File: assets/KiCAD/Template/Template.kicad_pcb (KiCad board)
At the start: 2 copper layers, 96.5 x 96.5 mm, 4 parts

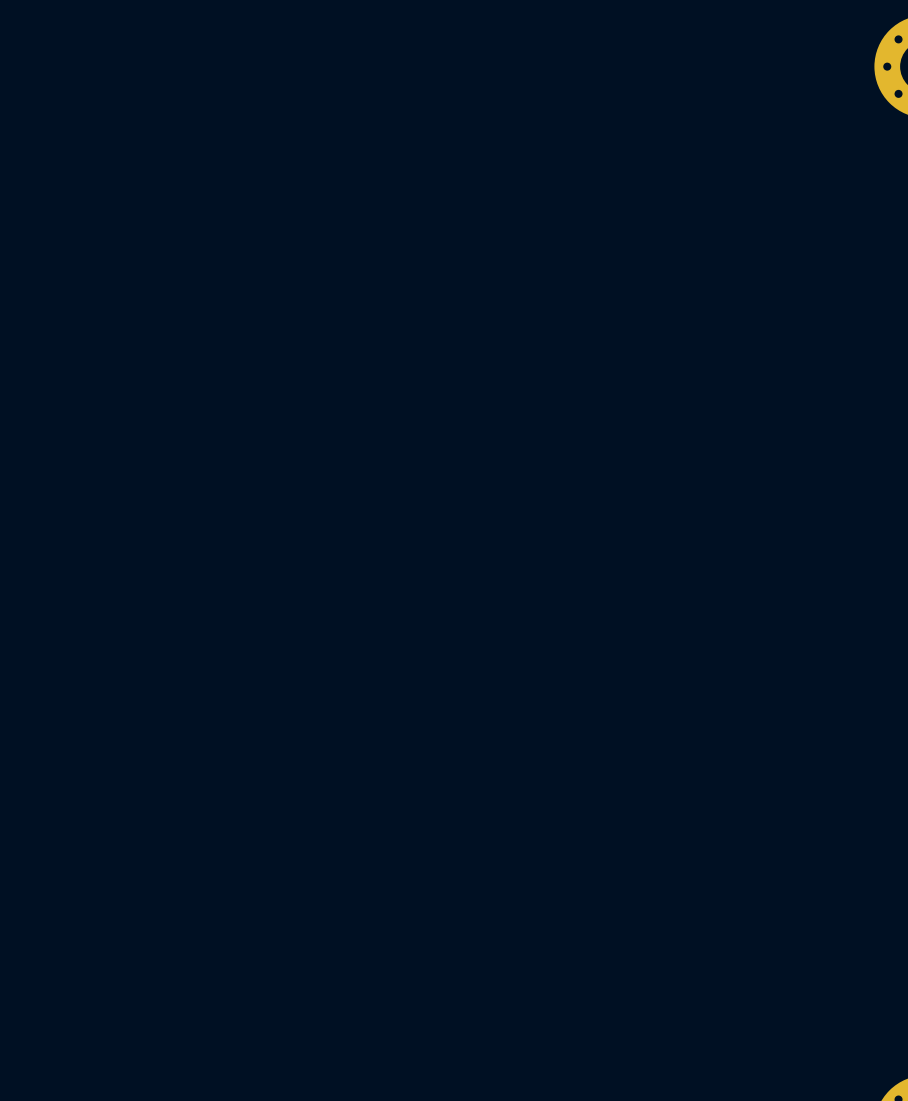
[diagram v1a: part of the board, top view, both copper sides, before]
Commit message: added terrain to opencl
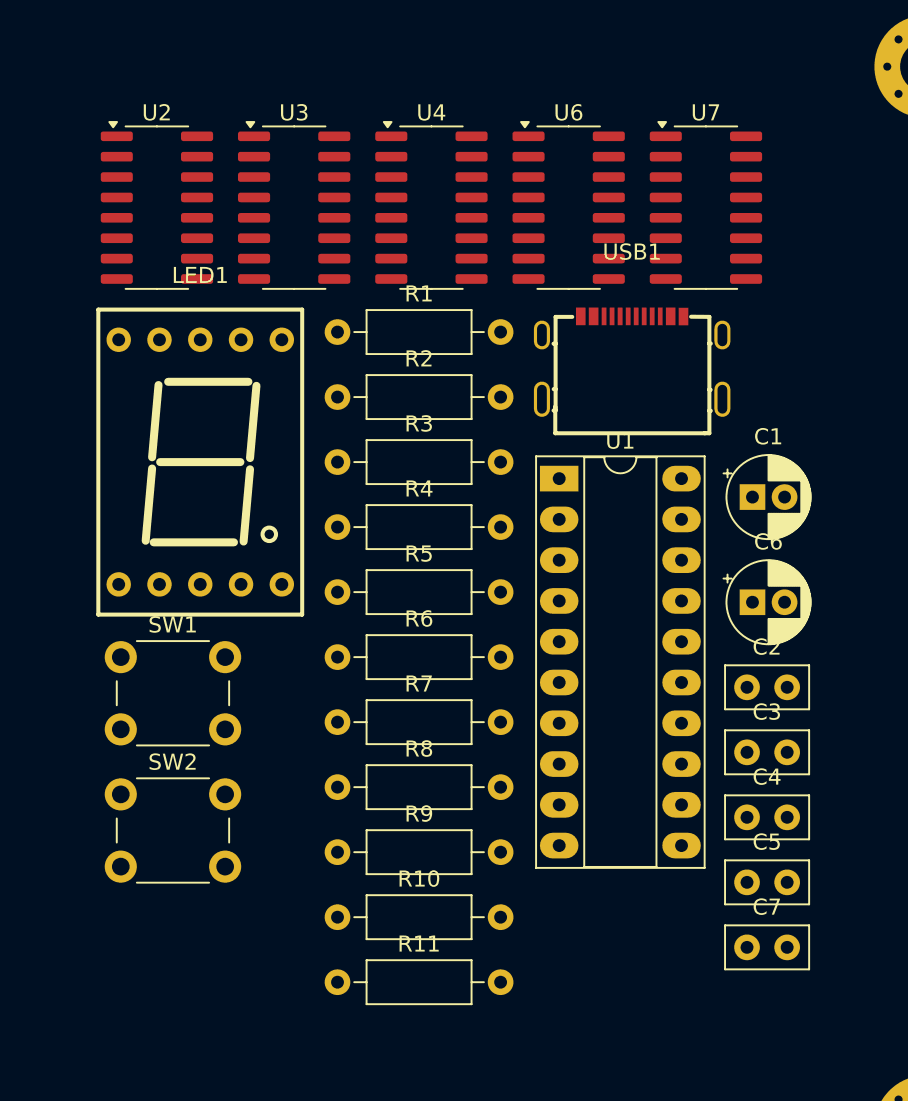
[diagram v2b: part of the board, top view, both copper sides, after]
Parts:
- added C1: 10uF, Capacitor_THT:CP_Radial_D5.0mm_P2.00mm, F.Cu at (172.1, 92.9)
- added C2: 1nF, Capacitor_THT:C_Disc_D5.0mm_W2.5mm_P2.50mm, F.Cu at (171.7, 104.7)
- added C3: 100nF, Capacitor_THT:C_Disc_D5.0mm_W2.5mm_P2.50mm, F.Cu at (171.7, 108.8)
- added C4: 100nF, Capacitor_THT:C_Disc_D5.0mm_W2.5mm_P2.50mm, F.Cu at (171.7, 112.8)
- added C5: 100nF, Capacitor_THT:C_Disc_D5.0mm_W2.5mm_P2.50mm, F.Cu at (171.7, 116.9)
- added C6: 10uF, Capacitor_THT:CP_Radial_D5.0mm_P2.00mm, F.Cu at (172.1, 99.4)
- added C7: 100nF, Capacitor_THT:C_Disc_D5.0mm_W2.5mm_P2.50mm, F.Cu at (171.7, 120.9)
- added LED1: SM410561N, EasyEDA:LED-SEG-TH_10P-L12.7-W19.0-P2.54-S15.24-BL, F.Cu at (137.7, 90.7)
- added R1: 470, Resistor_THT:R_Axial_DIN0207_L6.3mm_D2.5mm_P10.16mm_Horizontal, F.Cu at (146.2, 82.6)
- added R10: 10K, Resistor_THT:R_Axial_DIN0207_L6.3mm_D2.5mm_P10.16mm_Horizontal, F.Cu at (146.2, 119.0)
- added R11: 10K, Resistor_THT:R_Axial_DIN0207_L6.3mm_D2.5mm_P10.16mm_Horizontal, F.Cu at (146.2, 123.1)
- added R2: 470, Resistor_THT:R_Axial_DIN0207_L6.3mm_D2.5mm_P10.16mm_Horizontal, F.Cu at (146.2, 86.6)
- added R3: 470, Resistor_THT:R_Axial_DIN0207_L6.3mm_D2.5mm_P10.16mm_Horizontal, F.Cu at (146.2, 90.7)
- added R4: 470, Resistor_THT:R_Axial_DIN0207_L6.3mm_D2.5mm_P10.16mm_Horizontal, F.Cu at (146.2, 94.7)
- added R5: 470, Resistor_THT:R_Axial_DIN0207_L6.3mm_D2.5mm_P10.16mm_Horizontal, F.Cu at (146.2, 98.8)
- added R6: 470, Resistor_THT:R_Axial_DIN0207_L6.3mm_D2.5mm_P10.16mm_Horizontal, F.Cu at (146.2, 102.8)
- added R7: 470, Resistor_THT:R_Axial_DIN0207_L6.3mm_D2.5mm_P10.16mm_Horizontal, F.Cu at (146.2, 106.9)
- added R8: 5.1K, Resistor_THT:R_Axial_DIN0207_L6.3mm_D2.5mm_P10.16mm_Horizontal, F.Cu at (146.2, 110.9)
- added R9: 5.1K, Resistor_THT:R_Axial_DIN0207_L6.3mm_D2.5mm_P10.16mm_Horizontal, F.Cu at (146.2, 115.0)
- added SW1: BOOT, Button_Switch_THT:SW_PUSH_6mm, F.Cu at (132.7, 102.8)
- added SW2: RESET, Button_Switch_THT:SW_PUSH_6mm, F.Cu at (132.7, 111.4)
- added U1: ADC0820CCN, Package_DIP:DIP-20_W7.62mm_Socket_LongPads, F.Cu at (160.0, 91.7)
- added U2: 74LS47, Package_SO:SOP-16_3.9x9.9mm_P1.27mm, F.Cu at (135.0, 74.8)
- added U3: 74LS283, Package_SO:SOP-16_3.9x9.9mm_P1.27mm, F.Cu at (143.5, 74.8)
- added U4: CH552G, Package_SO:SOP-16_3.9x9.9mm_P1.27mm, F.Cu at (152.1, 74.8)
- added U6: 74HC165, Package_SO:SOP-16_3.9x9.9mm_P1.27mm, F.Cu at (160.6, 74.8)
- added U7: 74HC595, Package_SO:SOP-16_3.9x9.9mm_P1.27mm, F.Cu at (169.2, 74.8)
- added USB1: TYPEC, EasyEDA:USB-C-SMD_TYPEC-302-BRP16SC16, F.Cu at (164.6, 84.2)
